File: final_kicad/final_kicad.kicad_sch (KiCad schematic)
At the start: 71 parts, among them J3 Reflectance Sensor Array, M1 Motor, M3 Servo for Side Indicator, M4 Servo for Joint 1, M5 Motor_Step_4Wire, M6 Motor for Linear Actuator, M7 Servo for Joint 2, Q1 Photo_NPN, Q2 MOSFET-N, SW1 Reset, SW2 Reset, U1 SN754410, U2 MCP6294, U2 PIC32MX170F256B, U4 Comparator, U5 L293NE, U6 L293NE

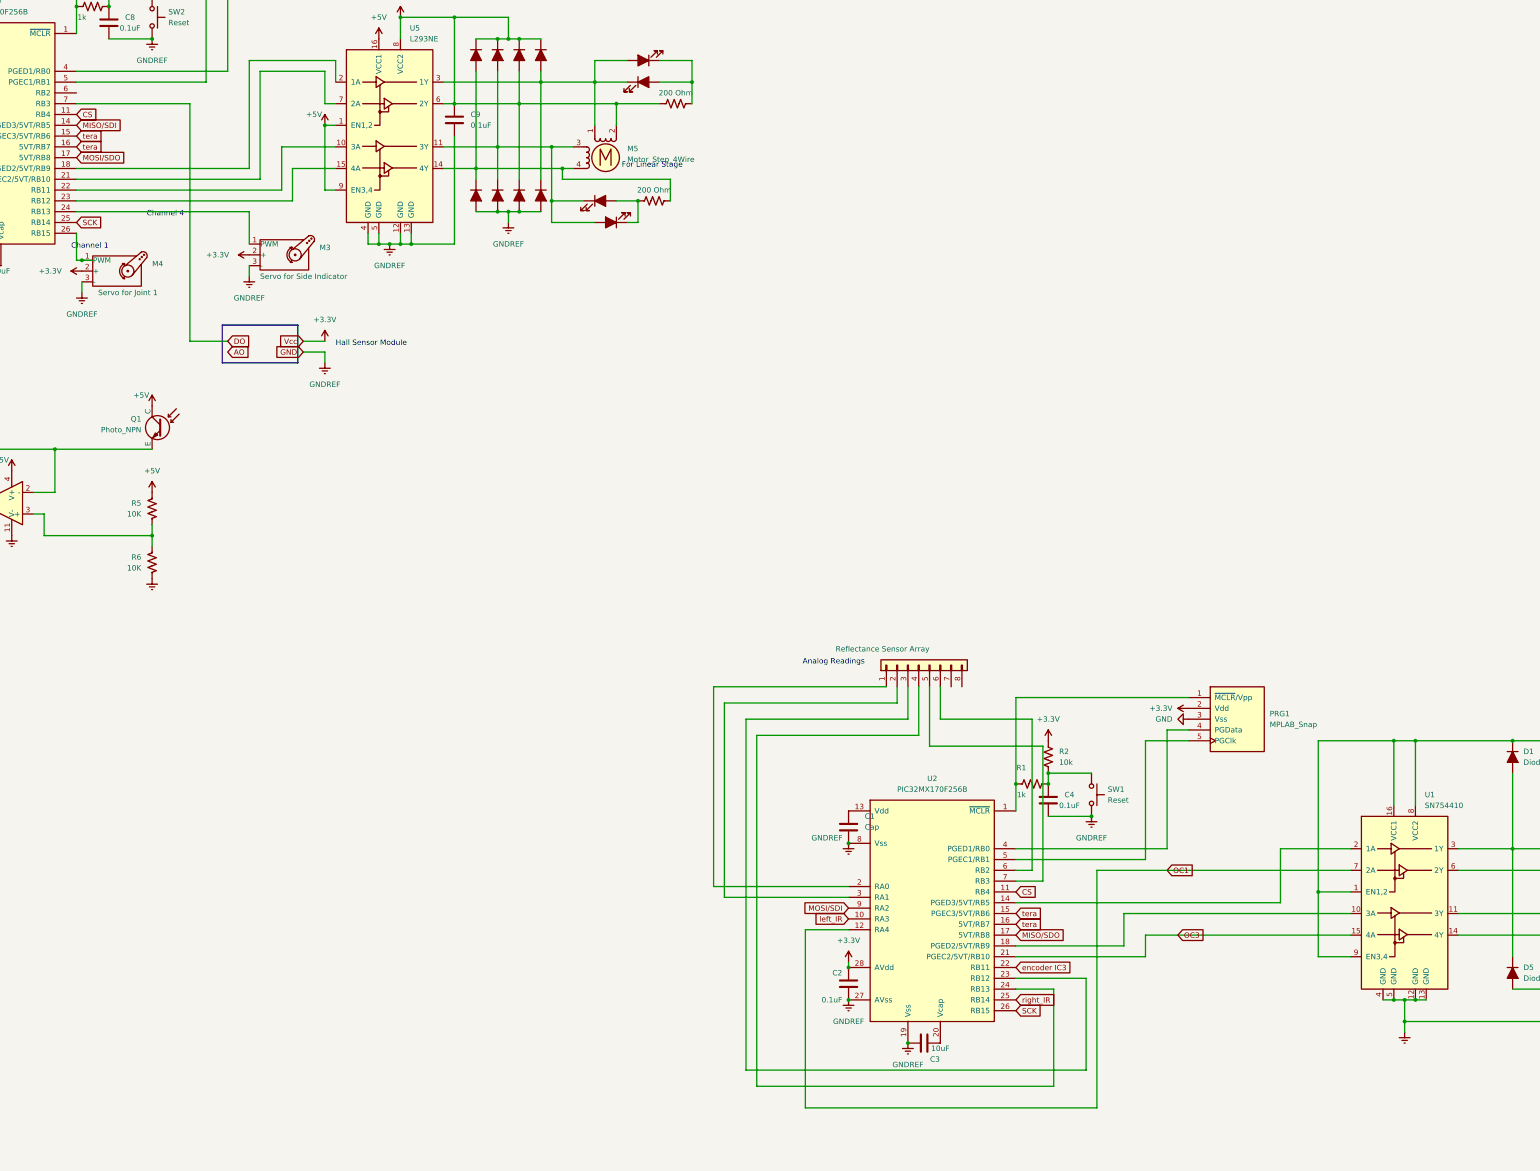
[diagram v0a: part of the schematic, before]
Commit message: update kicad for button and led and moved hall sensor to pic1
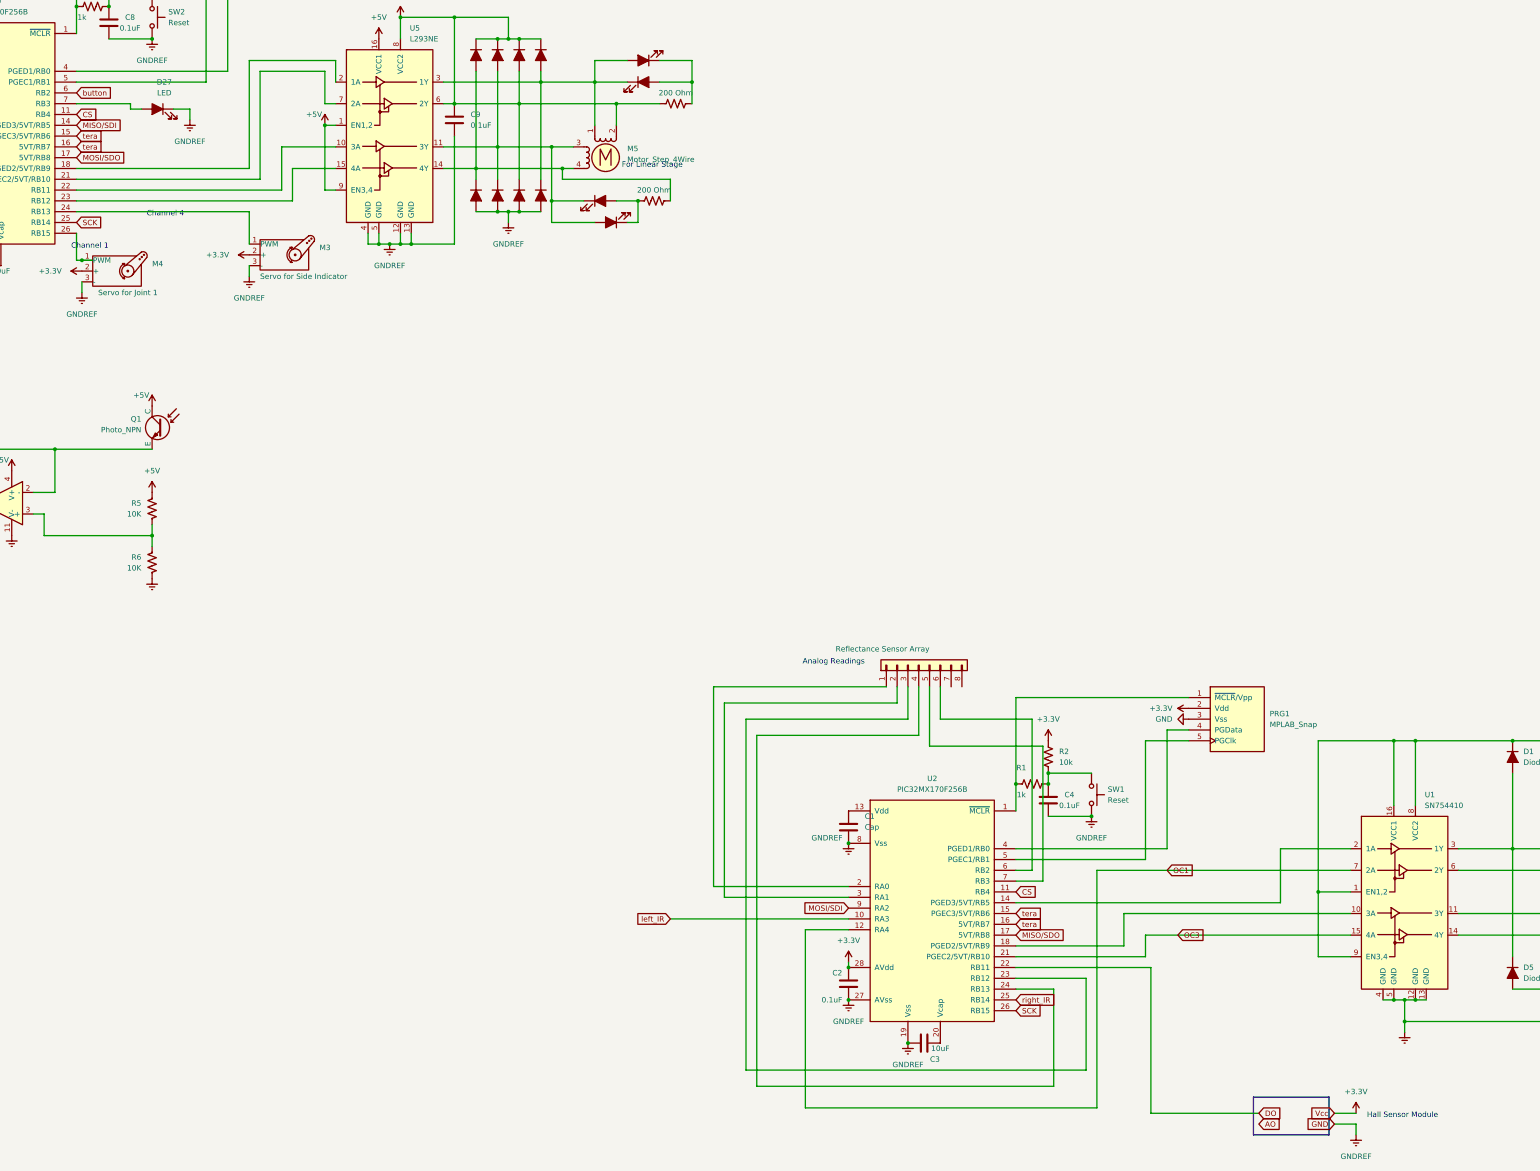
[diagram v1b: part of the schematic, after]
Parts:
- added D27: LED, symbol ME218_BaseLib:LED
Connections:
- net encoder IC3 is gone; now on net DO: U2.22 (RB11)
- net DO: no longer PIC0.7 (RB3)
- net GND: now also D27.1 (K)
- net button: now reaches PIC0.6 (RB2)
- new net: D27.2 (A), PIC0.7 (RB3)
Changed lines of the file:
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@@
     (stroke (width 0) (type default))
   )
+  (wire (pts (xy 363.22 294.64) (xy 394.97 294.64))
+    (stroke (width 0) (type default))
+  )
   (wire (pts (xy 38.1 78.74) (xy 50.8 78.74))
     (stroke (width 0) (type default))
@@
     (stroke (width 0) (type default))
   )
+  (wire (pts (xy 394.97 294.64) (xy 394.97 328.93))
+    (stroke (width 0) (type default))
+  )
   (wire (pts (xy 172.72 58.42) (xy 172.72 86.36))
     (stroke (width 0) (type default))
@@
     (stroke (width 0) (type default))
   )
+  (wire (pts (xy 142.24 91.44) (xy 154.94 91.44))
+    (stroke (width 0) (type default))
+  )
   (wire (pts (xy 182.88 129.54) (xy 182.88 132.08))
     (stroke (width 0) (type default))
@@
     (stroke (width 0) (type default))
   )
-  (wire (pts (xy 142.24 91.44) (xy 168.91 91.44))
-    (stroke (width 0) (type default))
-  )
   (wire (pts (xy 203.2 101.6) (xy 190.5 101.6))
     (stroke (width 0) (type default))
@@
     (stroke (width 0) (type default))
   )
-  (wire (pts (xy 177.8 147.32) (xy 168.91 147.32))
+  (wire (pts (xy 394.97 328.93) (xy 420.37 328.93))
     (stroke (width 0) (type default))
   )
@@
     (stroke (width 0) (type default))
   )
+  (wire (pts (xy 281.94 283.21) (xy 323.85 283.21))
+    (stroke (width 0) (type default))
+  )
   (wire (pts (xy 452.12 302.26) (xy 454.66 302.26))
     (stroke (width 0) (type default))
   )
+  (wire (pts (xy 165.1 92.71) (xy 168.91 92.71))
+    (stroke (width 0) (type default))
+  )
   (wire (pts (xy 38.1 88.9) (xy 38.1 78.74))
     (stroke (width 0) (type default))
@@
     (stroke (width 0) (type default))
   )
+  (wire (pts (xy 168.91 92.71) (xy 168.91 95.25))
+    (stroke (width 0) (type default))
+  )
   (wire (pts (xy 33.02 73.66) (xy 33.02 76.2))
     (stroke (width 0) (type default))
   )
+  (wire (pts (xy 154.94 91.44) (xy 154.94 92.71))
+    (stroke (width 0) (type default))
+  )
   (wire (pts (xy 86.36 100.33) (xy 86.36 130.81))
     (stroke (width 0) (type default))
@@
     (stroke (width 0) (type default))
   )
-  (wire (pts (xy 200.66 149.86) (xy 200.66 152.4))
+  (wire (pts (xy 443.23 331.47) (xy 443.23 334.01))
     (stroke (width 0) (type default))
   )
@@
     (stroke (width 0) (type default))
   )
-  (wire (pts (xy 195.58 147.32) (xy 200.66 147.32))
+  (wire (pts (xy 438.15 328.93) (xy 443.23 328.93))
     (stroke (width 0) (type default))
   )
@@
     (stroke (width 0) (type default))
   )
-  (wire (pts (xy 195.58 149.86) (xy 200.66 149.86))
+  (wire (pts (xy 438.15 331.47) (xy 443.23 331.47))
     (stroke (width 0) (type default))
   )
@@
     (stroke (width 0) (type default))
   )
+  (wire (pts (xy 154.94 92.71) (xy 157.48 92.71))
+    (stroke (width 0) (type default))
+  )
   (wire (pts (xy 102.87 82.55) (xy 102.87 83.82))
     (stroke (width 0) (type default))
@@
     (stroke (width 0) (type default))
   )
-  (wire (pts (xy 168.91 147.32) (xy 168.91 91.44))
-    (stroke (width 0) (type default))
-  )
   (wire (pts (xy 88.9 198.12) (xy 81.28 198.12))
     (stroke (width 0) (type default))
@@
     (stroke (width 0) (type default))
   )
-  (rectangle (start 176.53 143.51) (end 194.31 152.4)
+  (rectangle (start 419.1 325.12) (end 436.88 334.01)
     (stroke (width 0) (type default))
     (fill (type none))
@@
     (effects (font (size 1.27 1.27)) (justify left bottom))
   )
-  (text "Hall Sensor Module\n" (at 203.2 148.59 0)
+  (text "Hall Sensor Module\n" (at 445.77 330.2 0)
     (effects (font (size 1.27 1.27)) (justify left bottom))
   )
@@
     (effects (font (size 1.27 1.27)) (justify left bottom))
   )
-  (global_label "Vcc" (shape input) (at 195.58 147.32 180) (fields_autoplaced)
+  (global_label "Vcc" (shape input) (at 438.15 328.93 180) (fields_autoplaced)
     (effects (font (size 1.27 1.27)) (justify right))
-    (property "Intersheetrefs" "${INTERSHEET_REFS}" (at 189.329 147.32 0)
+    (property "Intersheetrefs" "${INTERSHEET_REFS}" (at 431.899 328.93 0)
       (effects (font (size 1.27 1.27)) (justify right) hide)
     )
   )
-  (global_label "encoder IC3" (shape input) (at 363.22 294.64 0) (fields_autoplaced)
-    (effects (font (size 1.27 1.27)) (justify left))
-    (property "Intersheetrefs" "${INTERSHEET_REFS}" (at 377.7561 294.64 0)
-      (effects (font (size 1.27 1.27)) (justify left) hide)
-    )
-  )
-  (global_label "left_IR" (shape input) (at 323.85 283.21 180) (fields_autoplaced)
+  (global_label "left_IR" (shape input) (at 281.94 283.21 180) (fields_autoplaced)
     (effects (font (size 1.27 1.27)) (justify right))
-    (property "Intersheetrefs" "${INTERSHEET_REFS}" (at 314.8172 283.21 0)
+    (property "Intersheetrefs" "${INTERSHEET_REFS}" (at 272.9072 283.21 0)
       (effects (font (size 1.27 1.27)) (justify right) hide)
     )
@@
     )
   )
+  (global_label "button" (shape input) (at 142.24 88.9 0) (fields_autoplaced)
+    (effects (font (size 1.27 1.27)) (justify left))
+    (property "Intersheetrefs" "${INTERSHEET_REFS}" (at 151.2726 88.9 0)
+      (effects (font (size 1.27 1.27)) (justify left) hide)
+    )
+  )
   (global_label "OC3" (shape input) (at 401.32 287.02 0) (fields_autoplaced)
     (effects (font (size 1.27 1.27)) (justify left))
@@
     )
   )
-  (global_label "DO" (shape input) (at 177.8 147.32 0) (fields_autoplaced)
+  (global_label "DO" (shape input) (at 420.37 328.93 0) (fields_autoplaced)
     (effects (font (size 1.27 1.27)) (justify left))
-    (property "Intersheetrefs" "${INTERSHEET_REFS}" (at 183.3857 147.32 0)
+    (property "Intersheetrefs" "${INTERSHEET_REFS}" (at 425.9557 328.93 0)
       (effects (font (size 1.27 1.27)) (justify left) hide)
     )
@@
     )
   )
-  (global_label "GND" (shape input) (at 195.58 149.86 180) (fields_autoplaced)
+  (global_label "GND" (shape input) (at 438.15 331.47 180) (fields_autoplaced)
     (effects (font (size 1.27 1.27)) (justify right))
-    (property "Intersheetrefs" "${INTERSHEET_REFS}" (at 188.7243 149.86 0)
+    (property "Intersheetrefs" "${INTERSHEET_REFS}" (at 431.2943 331.47 0)
       (effects (font (size 1.27 1.27)) (justify right) hide)
     )
@@
     )
   )
-  (global_label "AO" (shape input) (at 177.8 149.86 0) (fields_autoplaced)
+  (global_label "AO" (shape input) (at 420.37 331.47 0) (fields_autoplaced)
     (effects (font (size 1.27 1.27)) (justify left))
-    (property "Intersheetrefs" "${INTERSHEET_REFS}" (at 183.2043 149.86 0)
+    (property "Intersheetrefs" "${INTERSHEET_REFS}" (at 425.7743 331.47 0)
       (effects (font (size 1.27 1.27)) (justify left) hide)
     )
@@
     )
   )
+  (symbol (lib_id "ME218_BaseLib:LED") (at 161.29 92.71 0) (mirror y) (unit 1)
+    (in_bom yes) (on_board yes) (dnp no) (fields_autoplaced)
+    (property "Reference" "D27" (at 162.8902 86.36 0)
+      (effects (font (size 1.27 1.27)))
+    )
+    (property "Value" "LED" (at 162.8902 88.9 0)
+      (effects (font (size 1.27 1.27)))
+    )
+    (property "Footprint" "" (at 161.29 92.71 0)
+      (effects (font (size 1.27 1.27)) hide)
+    )
+    (property "Datasheet" "" (at 161.29 92.71 0)
+      (effects (font (size 1.27 1.27)) hide)
+    )
+    (pin "1")
+    (pin "2")
+    (instances
+      (project "final_kicad"
+        (path "/dd0cc16c-02d9-42f4-90a9-b5b59b4b5d24"
+          (reference "D27") (unit 1)
+        )
+      )
+    )
+  )
+  (symbol (lib_id "power:GNDREF") (at 168.91 95.25 0) (unit 1)
+    (in_bom yes) (on_board yes) (dnp no) (fields_autoplaced)
+    (property "Reference" "#PWR050" (at 168.91 101.6 0)
+      (effects (font (size 1.27 1.27)) hide)
+    )
+    (property "Value" "GNDREF" (at 168.91 100.33 0)
+      (effects (font (size 1.27 1.27)))
+    )
+    (property "Footprint" "" (at 168.91 95.25 0)
+      (effects (font (size 1.27 1.27)) hide)
+    )
+    (property "Datasheet" "" (at 168.91 95.25 0)
+      (effects (font (size 1.27 1.27)) hide)
+    )
+    (pin "1")
+    (instances
+      (project "final_kicad"
+        (path "/dd0cc16c-02d9-42f4-90a9-b5b59b4b5d24"
+          (reference "#PWR050") (unit 1)
+        )
+      )
+    )
+  )
   (symbol (lib_id "power:+3.3V") (at 143.51 130.81 90) (unit 1)
     (in_bom yes) (on_board yes) (dnp no)
@@
     )
   )
-  (symbol (lib_id "power:GNDREF") (at 200.66 152.4 0) (unit 1)
+  (symbol (lib_id "power:GNDREF") (at 443.23 334.01 0) (unit 1)
     (in_bom yes) (on_board yes) (dnp no)
-    (property "Reference" "#PWR036" (at 200.66 158.75 0)
+    (property "Reference" "#PWR036" (at 443.23 340.36 0)
       (effects (font (size 1.27 1.27)) hide)
     )
-    (property "Value" "GNDREF" (at 200.66 157.48 0)
+    (property "Value" "GNDREF" (at 443.23 339.09 0)
       (effects (font (size 1.27 1.27)))
     )
-    (property "Footprint" "" (at 200.66 152.4 0)
+    (property "Footprint" "" (at 443.23 334.01 0)
       (effects (font (size 1.27 1.27)) hide)
     )
-    (property "Datasheet" "" (at 200.66 152.4 0)
+    (property "Datasheet" "" (at 443.23 334.01 0)
       (effects (font (size 1.27 1.27)) hide)
     )
@@
     )
   )
-  (symbol (lib_id "power:+3.3V") (at 200.66 147.32 0) (unit 1)
+  (symbol (lib_id "power:+3.3V") (at 443.23 328.93 0) (unit 1)
     (in_bom yes) (on_board yes) (dnp no) (fields_autoplaced)
-    (property "Reference" "#PWR037" (at 200.66 151.13 0)
+    (property "Reference" "#PWR037" (at 443.23 332.74 0)
       (effects (font (size 1.27 1.27)) hide)
     )
-    (property "Value" "+3.3V" (at 200.66 142.24 0)
+    (property "Value" "+3.3V" (at 443.23 323.85 0)
       (effects (font (size 1.27 1.27)))
     )
-    (property "Footprint" "" (at 200.66 147.32 0)
+    (property "Footprint" "" (at 443.23 328.93 0)
       (effects (font (size 1.27 1.27)) hide)
     )
-    (property "Datasheet" "" (at 200.66 147.32 0)
+    (property "Datasheet" "" (at 443.23 328.93 0)
       (effects (font (size 1.27 1.27)) hide)
     )
